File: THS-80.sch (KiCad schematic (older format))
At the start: 25 parts, among them J1 USB_B_Micro, J2 RC80 Bus, J3 RC80 Expansion, J4 IDE, SW1 Reset, U1 MAX40203AUK, U2 DS1813R-5+T&R

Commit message: finished routing, drc passed
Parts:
- removed C4: 100nF, Capacitor_SMD:C_0603_1608Metric_Pad1.05x0.95mm_HandSolder, symbol THS-80-rescue:C_Small-Device-sbc_z80-rescue
- added C4: 100nF, Capacitor_SMD:C_0603_1608Metric_Pad1.05x0.95mm_HandSolder, symbol Device:C_Small
- added R14: 1K, Resistor_SMD:R_0603_1608Metric_Pad1.05x0.95mm_HandSolder, symbol Device:R_Small
- J4: footprint Connector_Multicomp:Multicomp_MC9A12-4034_2x20_P2.54mm_Vertical -> Connector_PinHeader_2.54mm:PinHeader_2x20_P2.54mm_Horizontal
- JP1: value Keypin -> PWR
- R6: value 1K -> 10K
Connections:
- wire segments 275 -> 272

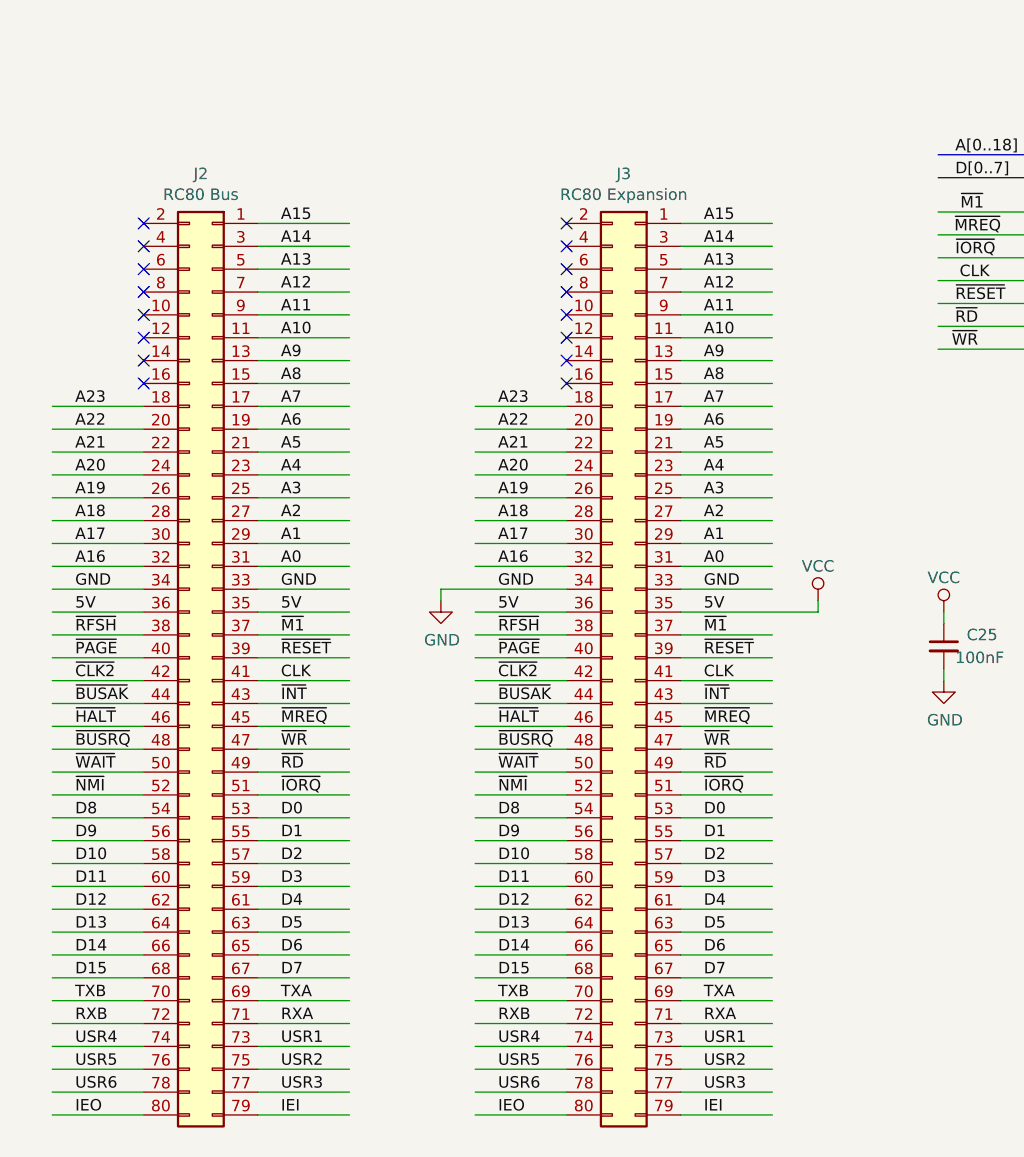
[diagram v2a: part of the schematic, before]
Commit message: fixed pmod pins
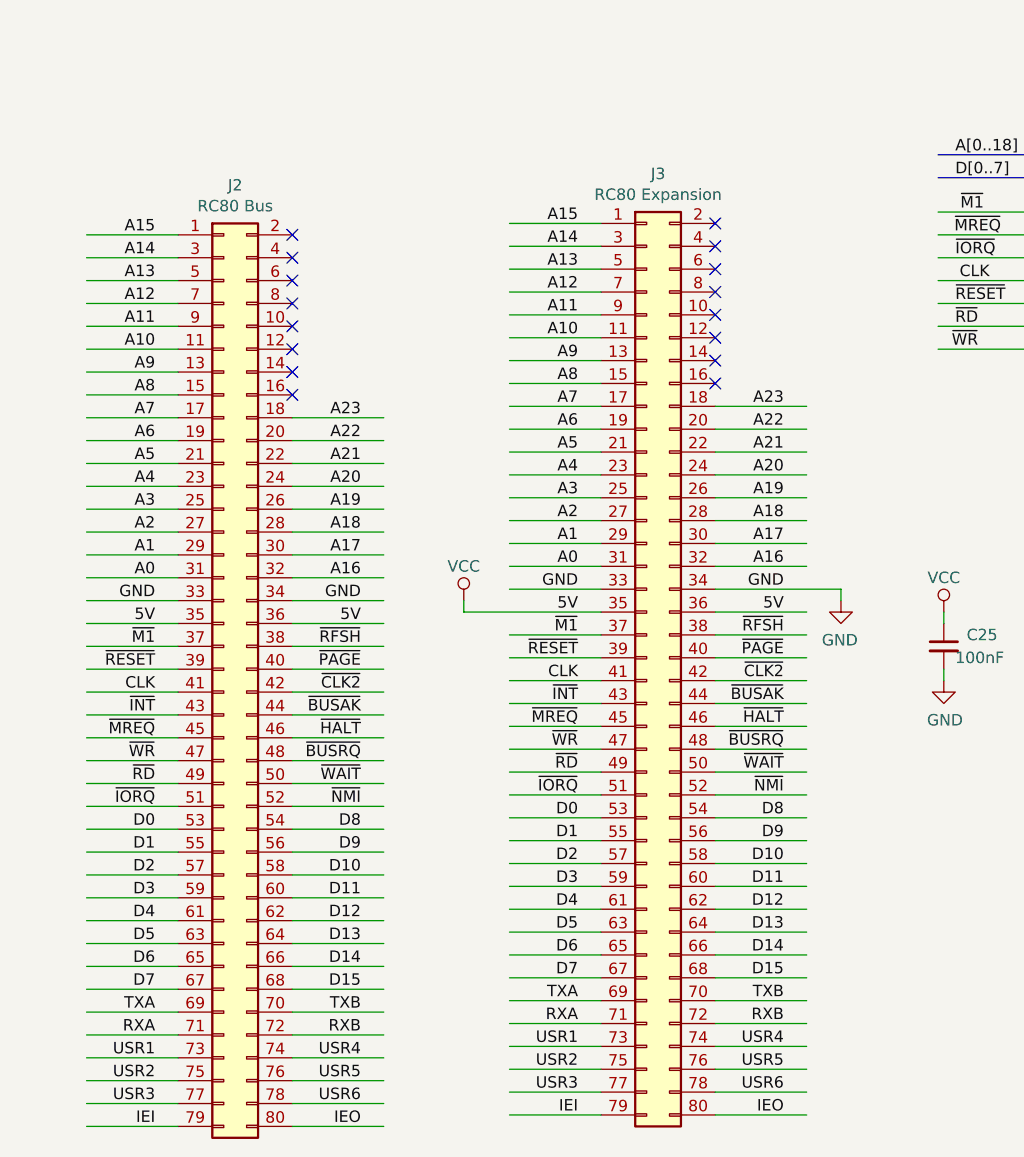
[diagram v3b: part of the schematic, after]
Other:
- moved on the sheet: J2, J3

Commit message: lots of fixes
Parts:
- removed C4: 100nF, Capacitor_SMD:C_0603_1608Metric_Pad1.05x0.95mm_HandSolder, symbol Device:C_Small
- removed D1: LED, LED_SMD:LED_0603_1608Metric_Pad1.05x0.95mm_HandSolder, symbol Device:LED
- removed J4: IDE, Connector_PinHeader_2.54mm:PinHeader_2x20_P2.54mm_Horizontal, symbol Connector_Generic:Conn_02x20_Odd_Even
- removed JP1: PWR, Connector_PinHeader_2.54mm:PinHeader_1x02_P2.54mm_Vertical, symbol Device:Jumper_NC_Small
- removed R14: 1K, Resistor_SMD:R_0603_1608Metric_Pad1.05x0.95mm_HandSolder, symbol Device:R_Small
- removed R6, R7, R8, R9: 10K, Resistor_SMD:R_0603_1608Metric_Pad1.05x0.95mm_HandSolder, symbol Device:R_Small
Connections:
- net labels added: A[0..2], IEO_2
- net labels removed: A[0..1], ~ACTIVE
- wire segments 272 -> 242
- no-connect marks 32 -> 19
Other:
- note removed: "IDE/CF"
- moved on the sheet: C25, R2, R3, R4, R5, SW1, U2

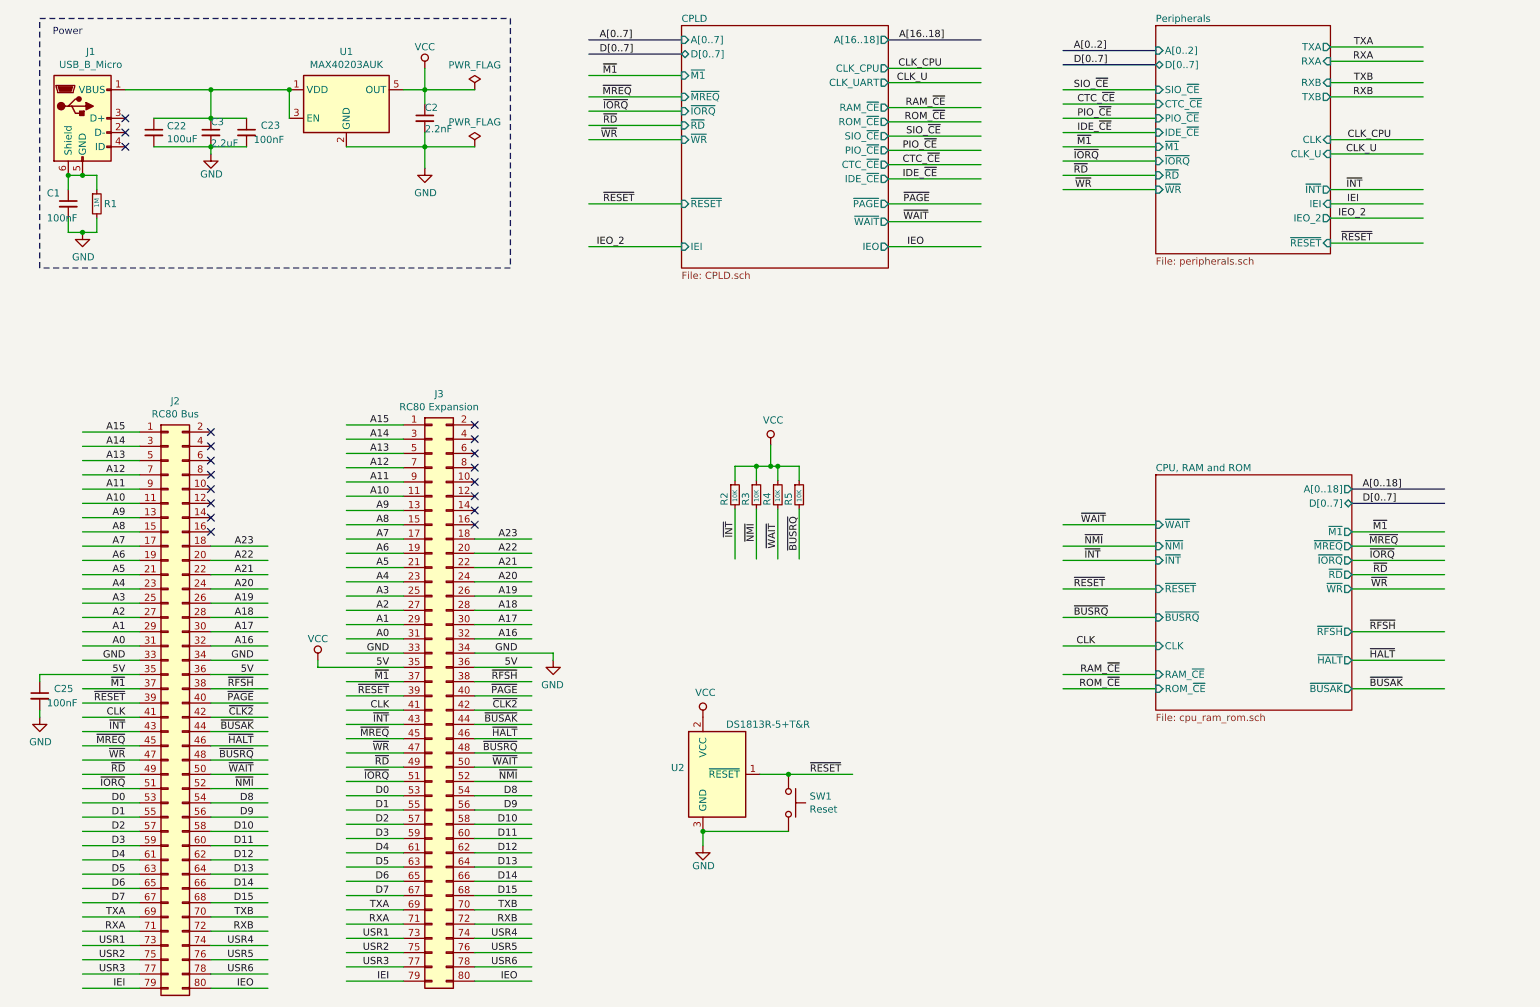
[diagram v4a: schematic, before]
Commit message: fixed led values, added pwr led
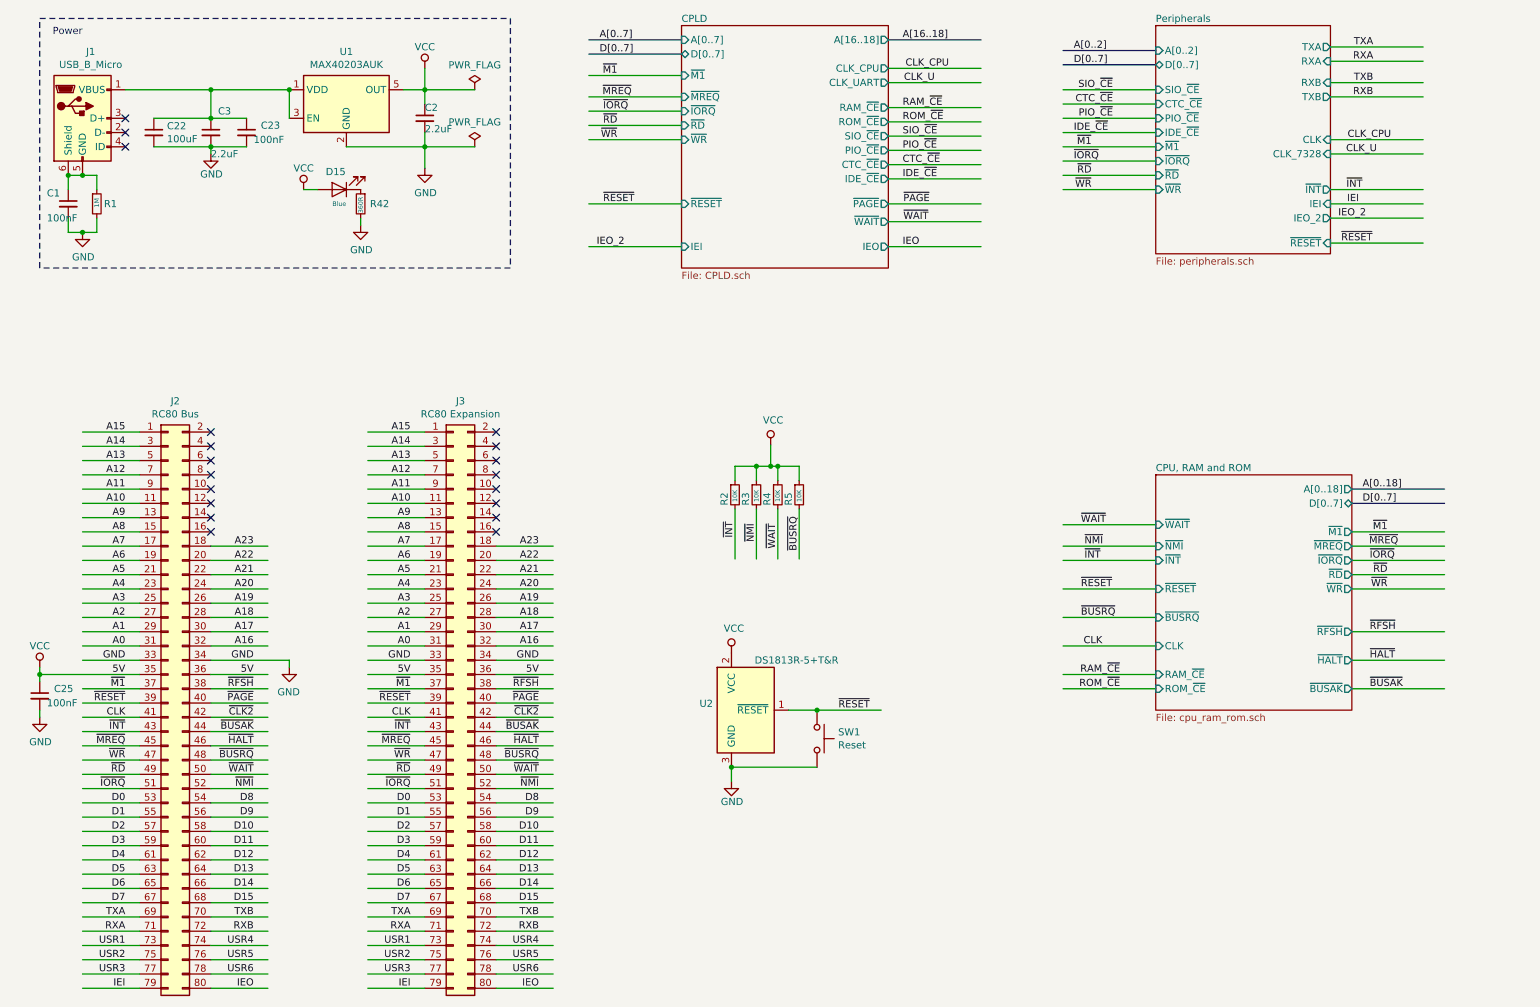
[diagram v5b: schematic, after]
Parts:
- added D15: Blue, LED_SMD:LED_0603_1608Metric_Pad1.05x0.95mm_HandSolder, symbol THS-80-rescue:LED-Device-max_breakout-rescue-sbc_z80-rescue
- added R42: 360R, Resistor_SMD:R_0603_1608Metric_Pad1.05x0.95mm_HandSolder, symbol Device:R_Small
- C2: value 2.2nF -> 2.2uF
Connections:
- wire segments 242 -> 244
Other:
- moved on the sheet: J3, SW1, U2

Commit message: fixes for CTC and additional clocks
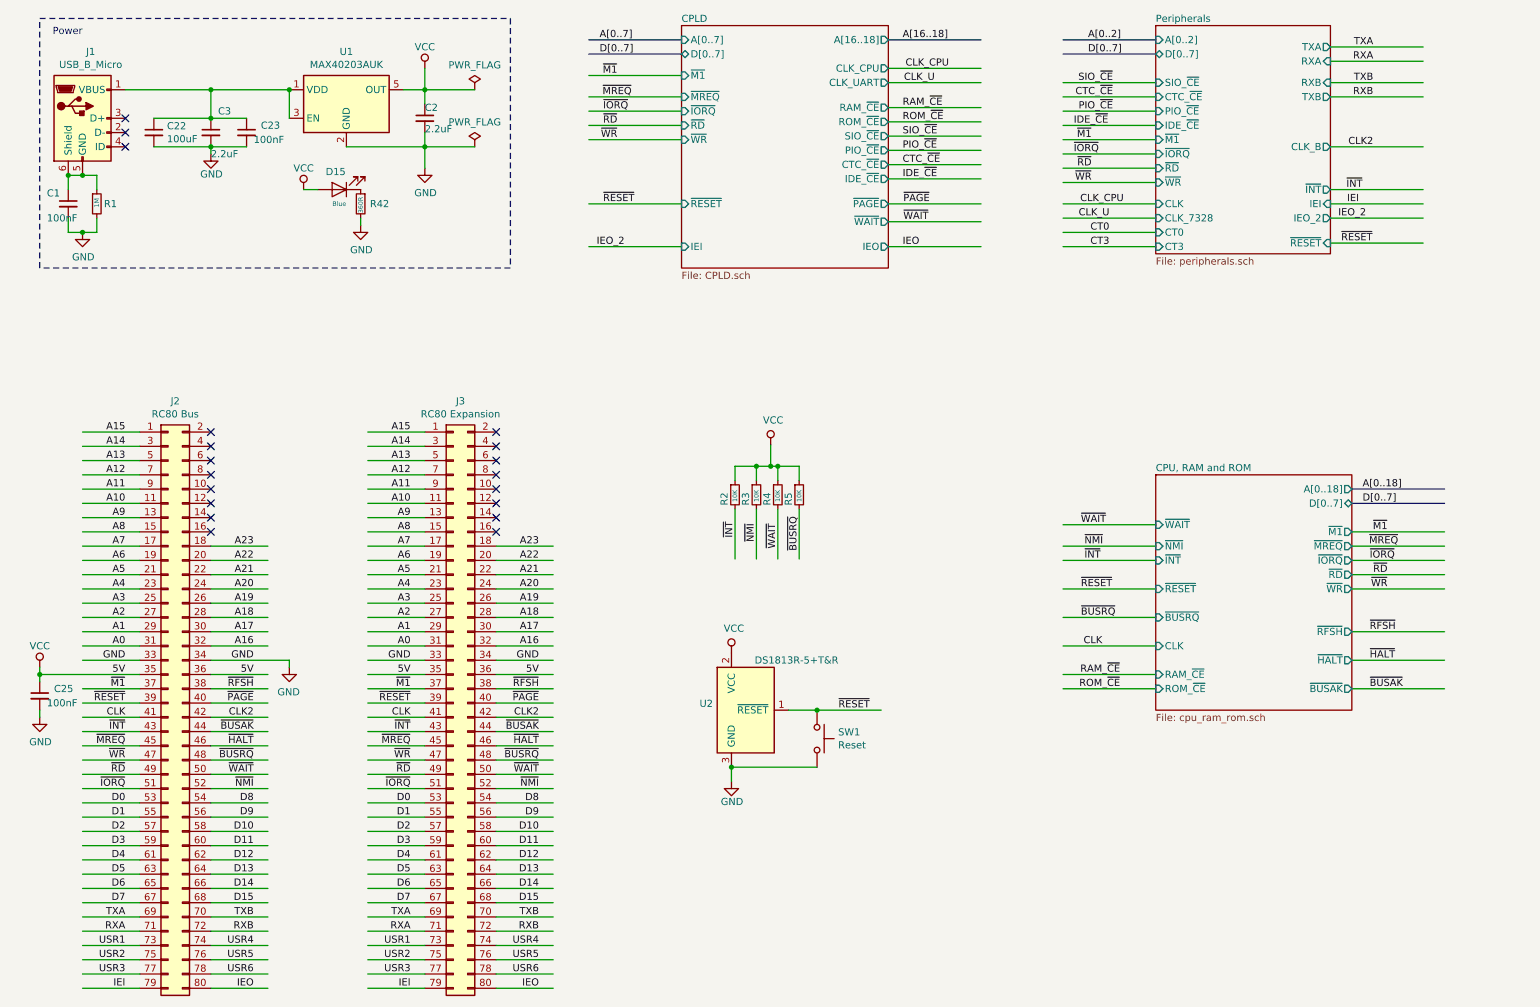
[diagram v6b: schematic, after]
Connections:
- net labels added: CLK2, CT0, CT3
- net labels removed: ~CLK2
- wire segments 244 -> 247
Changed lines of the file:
@@
 ~RFSH
 Text Label 4250 5650 2    50   ~ 0
-~CLK2
+CLK2
 Text Label 4250 5750 2    50   ~ 0
 ~BUSAK
@@
 ~RFSH
 Text Label 2250 5650 2    50   ~ 0
-~CLK2
+CLK2
 Text Label 2250 5750 2    50   ~ 0
 ~BUSAK
@@
 Wire Bus Line
 	5250 1000 4600 1000
-Text Label 8000 975  0    50   ~ 0
+Text Label 8100 900  0    50   ~ 0
 A[0..2]
-Text Label 8000 1075 0    50   ~ 0
+Text Label 8100 1000 0    50   ~ 0
 D[0..7]
 Wire Bus Line
-	8575 975  7925 975
-Wire Bus Line
-	8575 1075 7925 1075
+	8575 1000 7925 1000
 Text Label 10025 4050 0    50   ~ 0
 A[0..18]
@@
 Wire Wire Line
 	10600 4550 9950 4550
-$Sheet
-S 8575 800  1225 1600
-U 5DFE5C15
-F0 "Peripherals" 50
-F1 "peripherals.sch" 50
-F2 "A[0..2]" I L 8575 975 50
-F3 "CLK_7328" I R 9800 1700 50
-F4 "SIO_~CE~" I L 8575 1250 50
-F5 "~RESET~" I R 9800 2325 50
-F6 "~M1" I L 8575 1650 50
-F7 "~IORQ" I L 8575 1750 50
-F8 "~RD" I L 8575 1850 50
-F9 "CLK" I R 9800 1600 50
-F10 "IEI" I R 9800 2050 50
-F11 "CTC_~CE" I L 8575 1350 50
-F12 "PIO_~CE~" I L 8575 1450 50
-F13 "~INT" O R 9800 1950 50
-F14 "D[0..7]" T L 8575 1075 50
-F15 "IEO_2" O R 9800 2150 50
-F16 "IDE_~CE" I L 8575 1550 50
-F17 "~WR" I L 8575 1950 50
-F18 "TXA" O R 9800 950 50
-F19 "RXA" I R 9800 1050 50
-F20 "RXB" I R 9800 1200 50
-F21 "TXB" O R 9800 1300 50
-$EndSheet
-Text Label 8125 1650 2    50   ~ 0
-~M1
-Wire Wire Line
-	8575 1650 7925 1650
+Wire Wire Line
+	8575 1600 7925 1600
 Text Label 9875 2325 0    50   ~ 0
 ~RESET
@@
 	10450 2325 9800 2325
 Wire Wire Line
-	8575 1350 7925 1350
-Wire Wire Line
-	8575 1250 7925 1250
-Text Label 8275 1250 2    50   ~ 0
-SIO_~CE
-Text Label 8000 1750 0    50   ~ 0
-~IORQ
-Wire Wire Line
-	8575 1750 7925 1750
-Text Label 8125 1850 2    50   ~ 0
-~RD
-Wire Wire Line
-	8575 1850 7925 1850
-Wire Wire Line
-	10450 1600 9800 1600
-Wire Wire Line
-	10450 1700 9800 1700
+	8575 1300 7925 1300
+Wire Wire Line
+	8575 1200 7925 1200
+Wire Wire Line
+	8575 1700 7925 1700
+Wire Wire Line
+	8575 1800 7925 1800
+Wire Wire Line
+	8575 2050 7925 2050
+Wire Wire Line
+	8575 2150 7925 2150
 Wire Wire Line
 	10450 1950 9800 1950
@@
 Wire Wire Line
 	10450 2150 9800 2150
-Text Label 10125 1700 2    50   ~ 0
+Text Label 8250 2150 2    50   ~ 0
 CLK_U
-Text Label 10225 1600 2    50   ~ 0
+Text Label 8350 2050 2    50   ~ 0
 CLK_CPU
 Wire Wire Line
-	8575 1450 7925 1450
-Text Label 8275 1350 2    50   ~ 0
-CTC_~CE
-Text Label 8275 1450 2    50   ~ 0
-PIO_~CE
+	8575 1400 7925 1400
 Text Label 10075 5050 0    50   ~ 0
 ~RFSH
@@
 	750  5350 1450 5350
 Wire Wire Line
-	8575 1550 7925 1550
-Text Label 8000 1550 0    50   ~ 0
-IDE_~CE~
-Text Label 8125 1950 2    50   ~ 0
-~WR
-Wire Wire Line
-	8575 1950 7925 1950
+	8575 1500 7925 1500
+Wire Wire Line
+	8575 1900 7925 1900
 Wire Wire Line
 	9800 950  10450 950
@@
 	2600 1950 2700 1950
 Connection ~ 750  5350
+$Sheet
+S 8575 800  1225 1600
+U 5DFE5C15
+F0 "Peripherals" 50
+F1 "peripherals.sch" 50
+F2 "A[0..2]" I L 8575 900 50
+F3 "CLK_7328" I L 8575 2150 50
+F4 "SIO_~CE~" I L 8575 1200 50
+F5 "~RESET~" I R 9800 2325 50
+F6 "~M1" I L 8575 1600 50
+F7 "~IORQ" I L 8575 1700 50
+F8 "~RD" I L 8575 1800 50
+F9 "CLK" I L 8575 2050 50
+F10 "IEI" I R 9800 2050 50
+F11 "CTC_~CE" I L 8575 1300 50
+F12 "PIO_~CE~" I L 8575 1400 50
+F13 "~INT" O R 9800 1950 50
+F14 "D[0..7]" T L 8575 1000 50
+F15 "IEO_2" O R 9800 2150 50
+F16 "IDE_~CE" I L 8575 1500 50
+F17 "~WR" I L 8575 1900 50
+F18 "TXA" O R 9800 950 50
+F19 "RXA" I R 9800 1050 50
+F20 "RXB" I R 9800 1200 50
+F21 "TXB" O R 9800 1300 50
+F22 "CT0" I L 8575 2250 50
+F23 "CT3" I L 8575 2350 50
+F24 "CLK_B" O R 9800 1650 50
+$EndSheet
+Wire Wire Line
+	8575 2250 7925 2250
+Text Label 8250 2250 2    50   ~ 0
+CT0
+Wire Bus Line
+	8575 900  7925 900
+Text Label 8125 1900 2    50   ~ 0
+~WR
+Text Label 8000 1500 0    50   ~ 0
+IDE_~CE~
+Text Label 8275 1400 2    50   ~ 0
+PIO_~CE
+Text Label 8275 1300 2    50   ~ 0
+CTC_~CE
+Text Label 8125 1800 2    50   ~ 0
+~RD
+Text Label 8000 1700 0    50   ~ 0
+~IORQ
+Text Label 8275 1200 2    50   ~ 0
+SIO_~CE
+Text Label 8125 1600 2    50   ~ 0
+~M1
+Wire Wire Line
+	8575 2350 7925 2350
+Text Label 8250 2350 2    50   ~ 0
+CT3
+Wire Wire Line
+	9800 1650 10450 1650
+Text Label 10100 1650 2    50   ~ 0
+CLK2
 $EndSCHEMATC
